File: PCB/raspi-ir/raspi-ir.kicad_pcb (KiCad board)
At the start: 2 copper layers, 11.6 x 41 mm, 7 parts, among them J1 Conn_02x16_Odd_Even, J2 Conn_01x02_Pin, Q1 MMBT2222A, U1 TSOP382xx

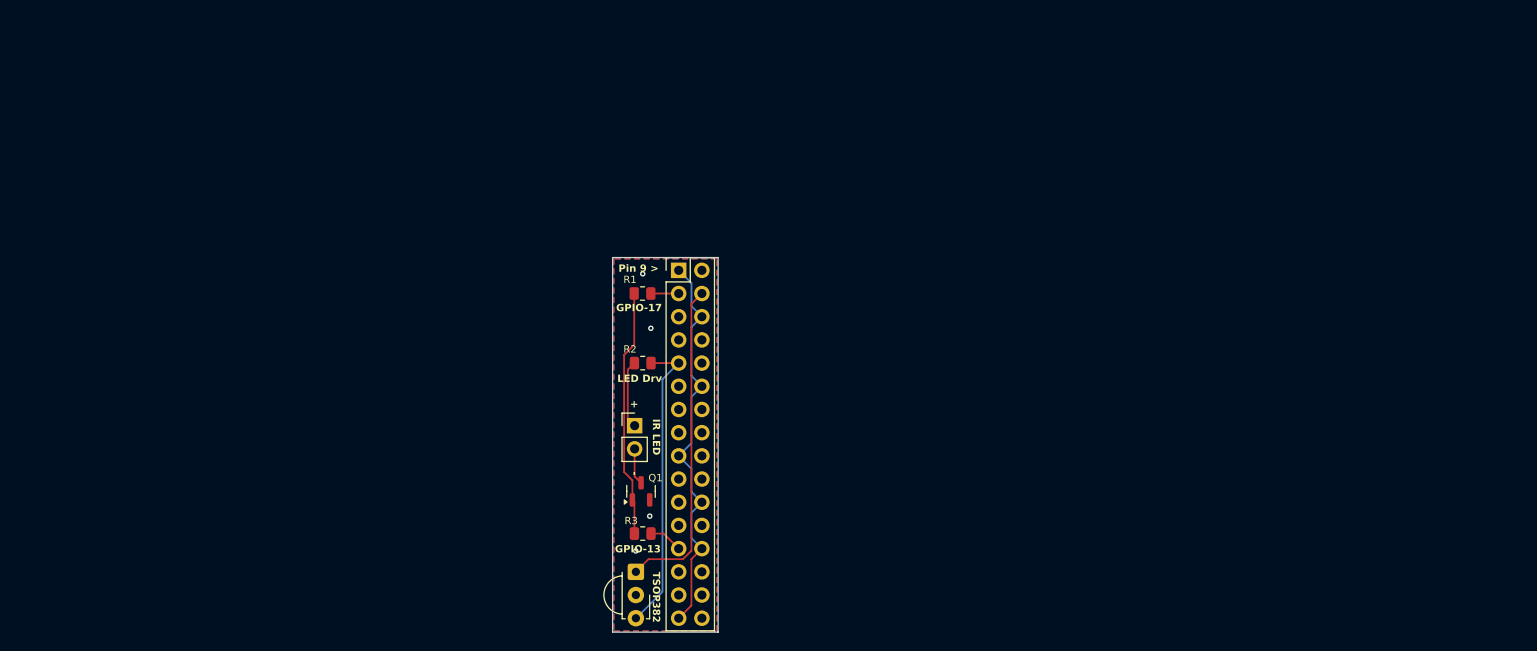
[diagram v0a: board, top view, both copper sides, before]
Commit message: Restructured icon files. Updating PCB with more features. Created conference room layout.
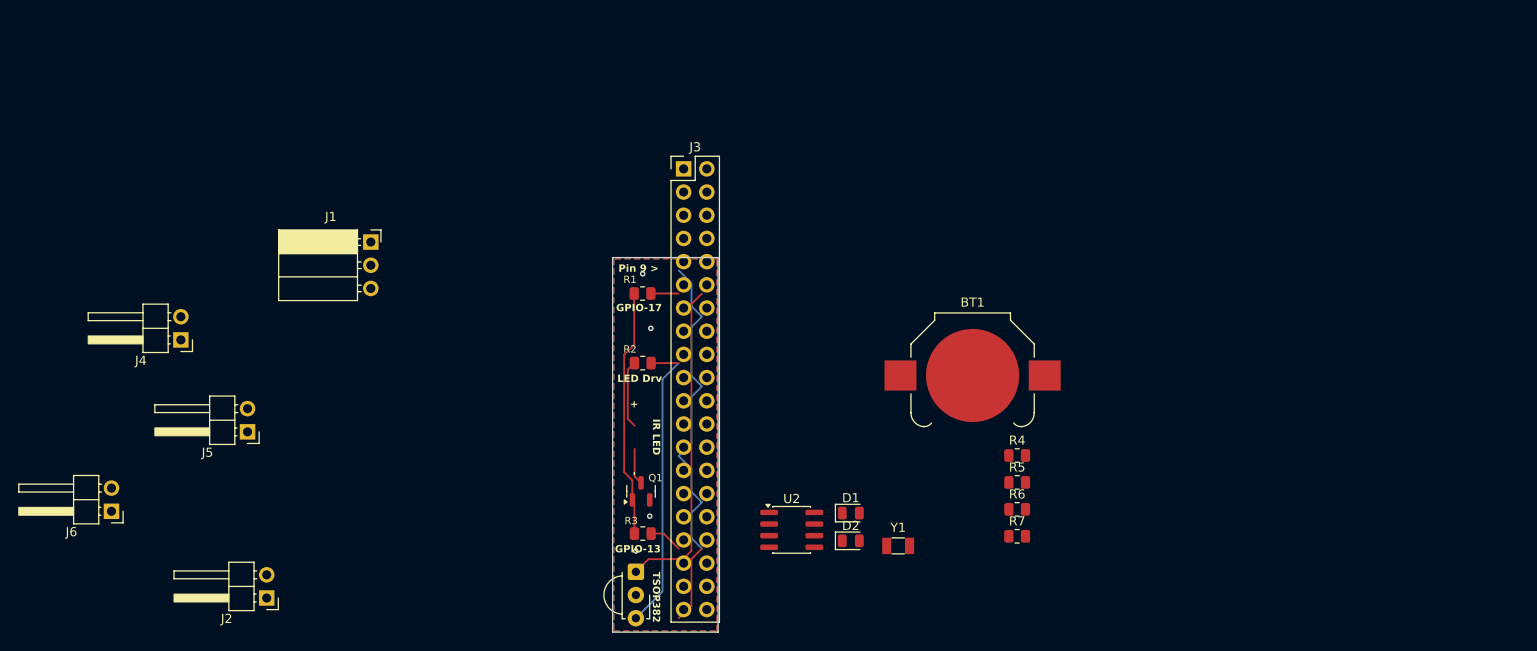
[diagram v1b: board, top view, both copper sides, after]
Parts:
- added BT1: Battery_Cell, Battery:BatteryHolder_Keystone_3000_1x12mm, F.Cu at (179.5, 84.3)
- added D1: LED, Diode_SMD:D_0805_2012Metric, F.Cu at (166.2, 99.4)
- added D2: LED, Diode_SMD:D_0805_2012Metric, F.Cu at (166.2, 102.4)
- added J3: Conn_02x20_Odd_Even, Connector_PinHeader_2.54mm:PinHeader_2x20_P2.54mm_Vertical, F.Cu at (147.9, 61.7)
- added J4: HR3P-N4EC-00000, Connector_PinHeader_2.54mm:PinHeader_1x02_P2.54mm_Horizontal, F.Cu at (92.8, 80.4)
- added J5: HR3P-N4EC-00000, Connector_PinHeader_2.54mm:PinHeader_1x02_P2.54mm_Horizontal, F.Cu at (100.1, 90.5)
- added J6: HR3P-N4EC-00000, Connector_PinHeader_2.54mm:PinHeader_1x02_P2.54mm_Horizontal, F.Cu at (85.2, 99.2)
- added R4: 47, Resistor_SMD:R_0805_2012Metric, F.Cu at (184.4, 93.0)
- added R5: 47, Resistor_SMD:R_0805_2012Metric, F.Cu at (184.4, 96.0)
- added R6: 47, Resistor_SMD:R_0805_2012Metric, F.Cu at (184.4, 99.0)
- added R7: 47, Resistor_SMD:R_0805_2012Metric, F.Cu at (184.4, 101.9)
- added U2: PCF8523T, Package_SO:SOIC-8_3.9x4.9mm_P1.27mm, F.Cu at (159.7, 101.2)
- added Y1: Crystal, Crystal:Crystal_SMD_3215-2Pin_3.2x1.5mm, F.Cu at (171.4, 103.0)
- J1: value Conn_02x16_Odd_Even -> Conn_01x03_Pin; footprint Connector_PinHeader_2.54mm:PinHeader_2x16_P2.54mm_Vertical -> Connector_PinSocket_2.54mm:PinSocket_1x03_P2.54mm_Horizontal
- J2: value Conn_01x02_Pin -> HR3P-N4EC-00000; footprint Connector_PinHeader_2.54mm:PinHeader_1x02_P2.54mm_Vertical -> Connector_PinHeader_2.54mm:PinHeader_1x02_P2.54mm_Horizontal
- R1: value R_US -> 1k
- R2: value R_US -> 47
- R3: value R_US -> EMPTY
- U1: value TSOP382xx -> TSOP38238
- moved J2 44.5 mm to (102.2, 108.7), turned to 180 degrees
- moved J1 33.9 mm to (113.6, 69.7)
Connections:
- J1 pad 1: GND -> Net-(J1-Pin_1)
- R1 pad 2: Net-(J1-Pin_3) -> Net-(J3-Pin_11)
- R3 pad 1: Net-(Q1-B) -> GND
- R3 pad 2: Net-(J1-Pin_25) -> Net-(D2-K)
- U1 pad 1: Net-(J1-Pin_4) -> Net-(D2-A)
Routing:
- net Net-(J1-Pin_4): track 35.7 -> 0.00 mm
- net Net-(D2-A): track 0.00 -> 35.7 mm
- net Net-(J1-Pin_25): track 3.71 -> 0.00 mm
- net Net-(D2-K): track 0.00 -> 3.71 mm
- net Net-(J3-Pin_11): track 0.00 -> 3.05 mm
- net Net-(J1-Pin_3): track 3.05 -> 0.00 mm

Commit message: Fix for fan position on case
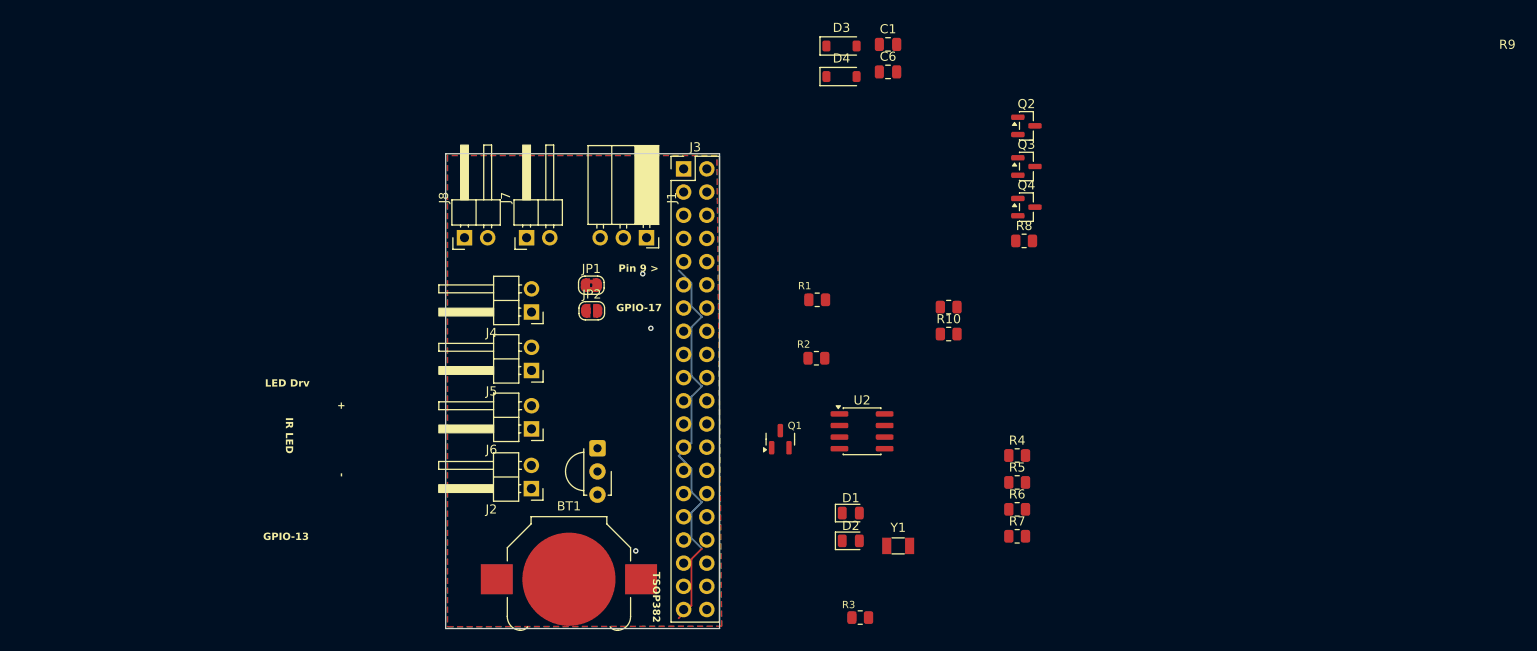
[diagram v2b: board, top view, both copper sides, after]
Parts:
- added C1: 10nF, Capacitor_SMD:C_0805_2012Metric, F.Cu at (170.2, 48.0)
- added C6: 10nF, Capacitor_SMD:C_0805_2012Metric, F.Cu at (170.2, 51.0)
- added D3: 1N4007FL, Diode_SMD:D_SOD-123, F.Cu at (165.2, 48.2)
- added D4: 1N4007FL, Diode_SMD:D_SOD-123, F.Cu at (165.2, 51.5)
- added J7: ~, Connector_PinHeader_2.54mm:PinHeader_1x02_P2.54mm_Horizontal, F.Cu at (130.7, 69.2)
- added J8: ~, Connector_PinHeader_2.54mm:PinHeader_1x02_P2.54mm_Horizontal, F.Cu at (123.9, 69.2)
- added JP1: SolderJumper_2_Bridged, Jumper:SolderJumper-2_P1.3mm_Bridged2Bar_RoundedPad1.0x1.5mm, F.Cu at (137.8, 74.4)
- added JP2: SolderJumper_2_Open, Jumper:SolderJumper-2_P1.3mm_Open_RoundedPad1.0x1.5mm, F.Cu at (137.8, 77.2)
- added Q2: MMBT2222A, Package_TO_SOT_SMD:SOT-23, F.Cu at (185.4, 57.0)
- added Q3: MMBT2222A, Package_TO_SOT_SMD:SOT-23, F.Cu at (185.4, 61.4)
- added Q4: MMBT2222A, Package_TO_SOT_SMD:SOT-23, F.Cu at (185.4, 65.8)
- added R10: 1k, Resistor_SMD:R_0805_2012Metric, F.Cu at (176.9, 79.8)
- added R8: 1k, Resistor_SMD:R_0805_2012Metric, F.Cu at (185.2, 69.5)
- added R9: 1k, Resistor_SMD:R_0805_2012Metric, F.Cu at (176.9, 76.8)
- R3: value EMPTY -> 470
- R7: value 47 -> 470
- moved BT1 49.5 mm to (135.3, 106.6)
- moved J6 46.9 mm to (131.2, 90.1)
- moved J4 38.5 mm to (131.2, 77.3)
- moved J5 31.8 mm to (131.2, 83.7)
- moved J2 31.4 mm to (131.2, 96.7)
- moved J1 30.2 mm to (143.8, 69.2), turned to -90 degrees
- moved R3 25.5 mm to (167.2, 110.8)
- moved R1 19.1 mm to (162.5, 76.0)
- moved R2 19.0 mm to (162.4, 82.4)
- moved Q1 16.3 mm to (158.4, 91.3)
- moved U1 14.2 mm to (138.4, 92.3)
- moved U2 13.3 mm to (167.4, 90.4)
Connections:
- net Net-(J1-Pin_3) renamed +5V
- J3 pad 3: unconnected-(J3-Pin_3-Pad3) -> Net-(J3-Pin_3)
- J3 pad 5: unconnected-(J3-Pin_5-Pad5) -> Net-(J3-Pin_5)
- J3 pad 8: unconnected-(J3-Pin_8-Pad8) -> Net-(J3-Pin_8)
- J5 pad 2: Net-(D1-K) -> Net-(J5-Pin_2)
- J6 pad 2: Net-(D1-K) -> Net-(J5-Pin_2)
- U2 pad 4: unconnected-(U2-VSS-Pad4) -> GND
- U2 pad 5: unconnected-(U2-SDA-Pad5) -> Net-(J3-Pin_3)
- U2 pad 6: unconnected-(U2-SCL-Pad6) -> Net-(J3-Pin_5)
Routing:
- net Net-(D2-A): track 35.7 -> 0.00 mm
- net +3.3V: track 32.9 -> 0.00 mm
- net Net-(Q1-B): track 27.2 -> 0.00 mm
- net Net-(J2-Pin_1): track 7.46 -> 0.00 mm
- net Net-(D1-K): track 4.01 -> 0.00 mm
- net Net-(D2-K): track 3.71 -> 0.00 mm
- net Net-(J3-Pin_11): track 3.05 -> 0.00 mm
- net GND: vias 4 -> 3
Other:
- board size 11.6 x 41 mm -> 30 x 52 mm

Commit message: Updated conference-room template, created install scripts, finished STL files.
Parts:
- removed JP1: SolderJumper_2_Bridged, Jumper:SolderJumper-2_P1.3mm_Bridged2Bar_RoundedPad1.0x1.5mm
- removed JP2: SolderJumper_2_Open, Jumper:SolderJumper-2_P1.3mm_Open_RoundedPad1.0x1.5mm
- moved Q2 52.3 mm to (137.0, 76.6)
- moved Q3 52.3 mm to (137.0, 81.0)
- moved Q4 52.3 mm to (137.0, 85.5)
- moved R8 52.3 mm to (136.7, 89.2)
- moved D3 46.7 mm to (125.1, 72.2)
- moved R5 44.9 mm to (143.8, 76.8)
- moved R6 44.9 mm to (143.8, 79.8)
- moved R7 44.9 mm to (143.8, 82.8)
- moved R4 44.9 mm to (143.8, 73.9)
- moved D1 41.1 mm to (133.5, 74.4)
- moved C1 40.2 mm to (139.4, 73.8)
- moved C6 40.2 mm to (139.4, 76.8)
- moved D2 39.3 mm to (133.5, 80.6)
- moved D4 39.2 mm to (131.8, 72.2)
- moved R3 38.2 mm to (134.5, 91.1)
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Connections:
- D3 pad 1: Net-(D3-K) -> +3.3V
- D4 pad 1: Net-(D3-K) -> +3.3V
- J7 pad 1: Net-(D3-K) -> +3.3V
- J8 pad 1: Net-(D3-K) -> +3.3V
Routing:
- net GND: vias 3 -> 1
